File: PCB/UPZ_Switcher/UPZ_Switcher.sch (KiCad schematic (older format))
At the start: 0 parts

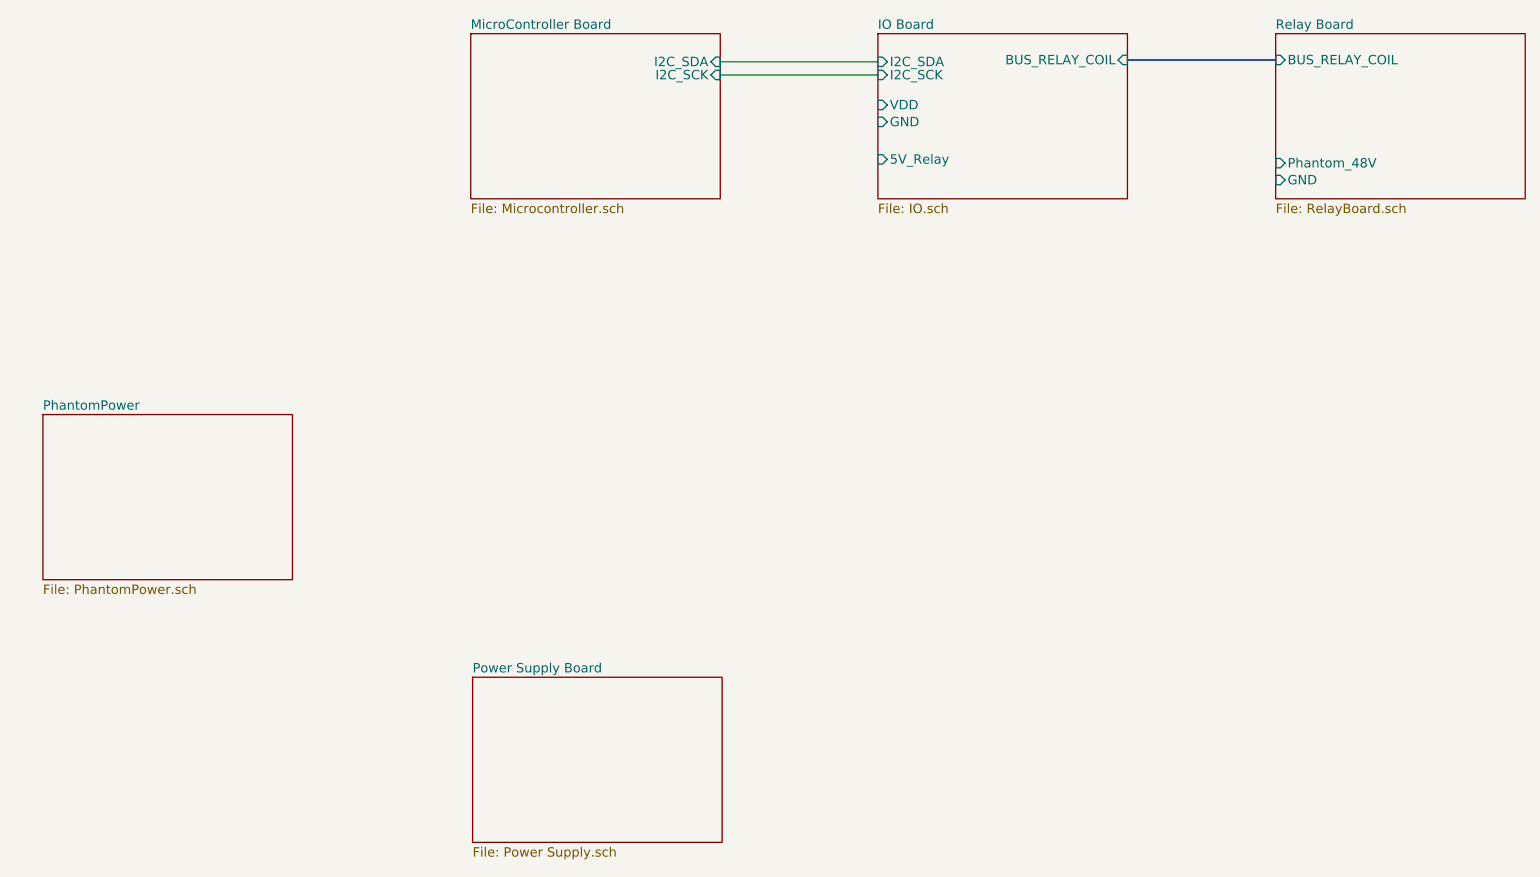
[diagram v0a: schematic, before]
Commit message: Updated schematic, PSU added + draft program
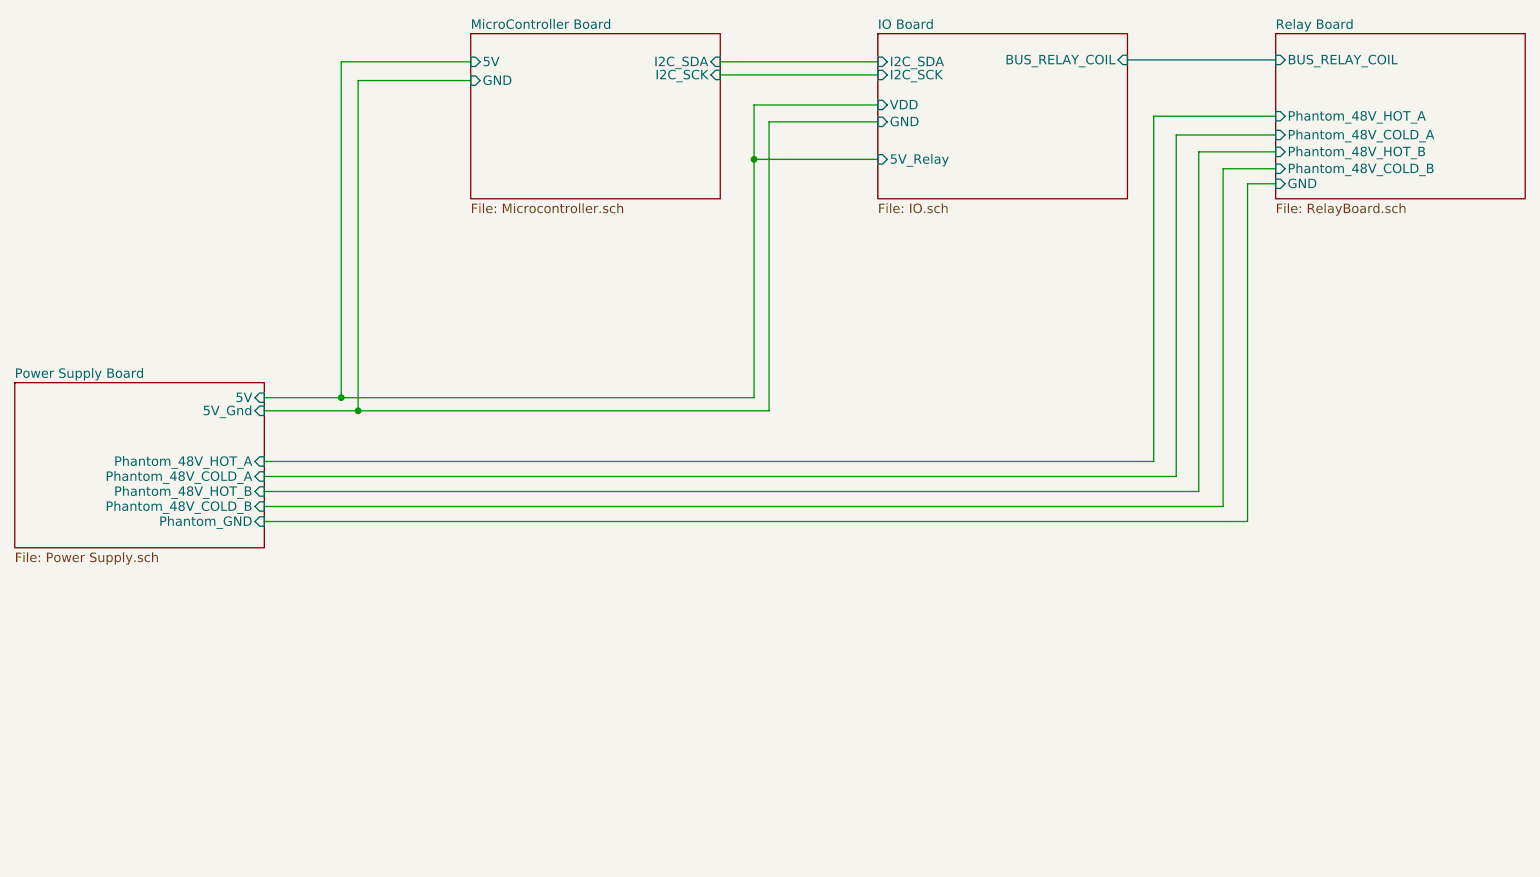
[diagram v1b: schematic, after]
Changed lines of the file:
@@
 $Descr A4 11693 8268
 encoding utf-8
-Sheet 1 6
+Sheet 1 5
 Title ""
 Date ""
@@
 F2 "I2C_SCK" I R 5270 1730 50
 F3 "I2C_SDA" I R 5270 1660 50
+F4 "5V" I L 3940 1660 50
+F5 "GND" I L 3940 1760 50
 $EndSheet
 $Sheet
-S 3950 4940 1330 880
+S 1510 3370 1330 880
 U 62E5E929
 F0 "Power Supply Board" 50
 F1 "Power Supply.sch" 50
+F2 "Phantom_48V_COLD_A" I R 2840 3870 50
+F3 "Phantom_48V_HOT_A" I R 2840 3790 50
+F4 "Phantom_48V_COLD_B" I R 2840 4030 50
+F5 "Phantom_48V_HOT_B" I R 2840 3950 50
+F6 "5V" I R 2840 3450 50
+F7 "Phantom_GND" I R 2840 4110 50
+F8 "5V_Gnd" I R 2840 3520 50
 $EndSheet
 $Sheet
@@
 F0 "Relay Board" 50
 F1 "RelayBoard.sch" 50
-F2 "Phantom_48V" I L 8230 2200 50
-F3 "BUS_RELAY_COIL" I L 8230 1650 50
-F4 "GND" I L 8230 2290 50
-$EndSheet
-$Sheet
-S 1660 3540 1330 880
-U 62E8A761
-F0 "PhantomPower" 50
-F1 "PhantomPower.sch" 50
+F2 "BUS_RELAY_COIL" I L 8230 1650 50
+F3 "GND" I L 8230 2310 50
+F4 "Phantom_48V_HOT_A" I L 8230 1950 50
+F5 "Phantom_48V_COLD_A" I L 8230 2050 50
+F6 "Phantom_48V_HOT_B" I L 8230 2140 50
+F7 "Phantom_48V_COLD_B" I L 8230 2230 50
 $EndSheet
 Wire Bus Line
@@
 Wire Wire Line
 	5270 1730 6110 1730
+Wire Wire Line
+	2840 3790 7580 3790
+Wire Wire Line
+	7580 3790 7580 1950
+Wire Wire Line
+	7580 1950 8230 1950
+Wire Wire Line
+	8230 2050 7700 2050
+Wire Wire Line
+	7700 2050 7700 3870
+Wire Wire Line
+	7700 3870 2840 3870
+Wire Wire Line
+	2840 3950 7820 3950
+Wire Wire Line
+	7820 3950 7820 2140
+Wire Wire Line
+	7820 2140 8230 2140
+Wire Wire Line
+	2840 4030 7950 4030
+Wire Wire Line
+	7950 4030 7950 2230
+Wire Wire Line
+	7950 2230 8230 2230
+Wire Wire Line
+	8230 2310 8080 2310
+Wire Wire Line
+	8080 2310 8080 4110
+Wire Wire Line
+	8080 4110 2840 4110
+Wire Wire Line
+	2840 3450 3250 3450
+Wire Wire Line
+	3250 3450 3250 1660
+Wire Wire Line
+	3250 1660 3940 1660
+Wire Wire Line
+	2840 3520 3340 3520
+Wire Wire Line
+	3340 3520 3340 1760
+Wire Wire Line
+	3340 1760 3940 1760
+Wire Wire Line
+	6110 1890 5450 1890
+Wire Wire Line
+	5450 1890 5450 2180
+Wire Wire Line
+	5450 3450 3250 3450
+Connection ~ 3250 3450
+Wire Wire Line
+	6110 1980 5530 1980
+Wire Wire Line
+	5530 1980 5530 3520
+Wire Wire Line
+	5530 3520 3340 3520
+Connection ~ 3340 3520
+Wire Wire Line
+	6110 2180 5450 2180
+Connection ~ 5450 2180
+Wire Wire Line
+	5450 2180 5450 3450
 $EndSCHEMATC

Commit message: Started PCB design
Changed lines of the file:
@@
 $Descr A4 11693 8268
 encoding utf-8
-Sheet 1 5
+Sheet 1 6
 Title ""
 Date ""
@@
 Comment4 ""
 $EndDescr
-$Sheet
-S 6110 1510 1330 880
-U 62DF27C2
-F0 "IO Board" 50
-F1 "IO.sch" 50
-F2 "BUS_RELAY_COIL" I R 7440 1650 50
-F3 "5V_Relay" I L 6110 2180 50
-F4 "I2C_SDA" I L 6110 1660 50
-F5 "I2C_SCK" I L 6110 1730 50
-F6 "VDD" I L 6110 1890 50
-F7 "GND" I L 6110 1980 50
-$EndSheet
 $Sheet
 S 3940 1510 1330 880
@@
 F8 "5V_Gnd" I R 2840 3520 50
 $EndSheet
-$Sheet
-S 8230 1510 1330 880
-U 62E5E978
-F0 "Relay Board" 50
-F1 "RelayBoard.sch" 50
-F2 "BUS_RELAY_COIL" I L 8230 1650 50
-F3 "GND" I L 8230 2310 50
-F4 "Phantom_48V_HOT_A" I L 8230 1950 50
-F5 "Phantom_48V_COLD_A" I L 8230 2050 50
-F6 "Phantom_48V_HOT_B" I L 8230 2140 50
-F7 "Phantom_48V_COLD_B" I L 8230 2230 50
-$EndSheet
-Wire Bus Line
-	7440 1650 8230 1650
 Wire Wire Line
-	5270 1660 6110 1660
+	2840 3790 5600 3790
 Wire Wire Line
-	5270 1730 6110 1730
+	2840 3950 5760 3950
 Wire Wire Line
-	2840 3790 7580 3790
-Wire Wire Line
-	7580 3790 7580 1950
-Wire Wire Line
-	7580 1950 8230 1950
-Wire Wire Line
-	8230 2050 7700 2050
-Wire Wire Line
-	7700 2050 7700 3870
-Wire Wire Line
-	7700 3870 2840 3870
-Wire Wire Line
-	2840 3950 7820 3950
-Wire Wire Line
-	7820 3950 7820 2140
-Wire Wire Line
-	7820 2140 8230 2140
-Wire Wire Line
-	2840 4030 7950 4030
-Wire Wire Line
-	7950 4030 7950 2230
-Wire Wire Line
-	7950 2230 8230 2230
-Wire Wire Line
-	8230 2310 8080 2310
-Wire Wire Line
-	8080 2310 8080 4110
-Wire Wire Line
-	8080 4110 2840 4110
+	2840 4030 5840 4030
 Wire Wire Line
 	2840 3450 3250 3450
@@
 	3340 1760 3940 1760
 Wire Wire Line
-	6110 1890 5450 1890
-Wire Wire Line
-	5450 1890 5450 2180
-Wire Wire Line
-	5450 3450 3250 3450
+	5440 3450 3250 3450
 Connection ~ 3250 3450
 Wire Wire Line
-	6110 1980 5530 1980
+	5520 3520 3340 3520
+Connection ~ 3340 3520
+$Sheet
+S 6110 2730 1330 880
+U 604B7458
+F0 "Main Relay Board" 50
+F1 "Main_Relay_Board.sch" 50
+F2 "Phantom_48V_HOT_A" I L 6110 3230 50
+F3 "Phantom_48V_COLD_A" I L 6110 3310 50
+F4 "Phantom_48V_HOT_B" I L 6110 3390 50
+F5 "Phantom_48V_COLD_B" I L 6110 3470 50
+F6 "Phantom_GND" I L 6110 3550 50
+F7 "I2C_SDA" I L 6110 2820 50
+F8 "I2C_SCK" I L 6110 2900 50
+F9 "VDD" I L 6110 2990 50
+F10 "GND" I L 6110 3070 50
+F11 "5V_Relay" I L 6110 3150 50
+$EndSheet
 Wire Wire Line
-	5530 1980 5530 3520
+	6110 3150 5440 3150
 Wire Wire Line
-	5530 3520 3340 3520
-Connection ~ 3340 3520
+	6110 3070 5520 3070
 Wire Wire Line
-	6110 2180 5450 2180
-Connection ~ 5450 2180
+	5520 3070 5520 3520
 Wire Wire Line
-	5450 2180 5450 3450
+	6110 3230 5600 3230
+Wire Wire Line
+	5600 3230 5600 3790
+Wire Wire Line
+	6110 3310 5680 3310
+Wire Wire Line
+	5680 3310 5680 3870
+Wire Wire Line
+	5680 3870 2840 3870
+Wire Wire Line
+	6110 3390 5760 3390
+Wire Wire Line
+	5760 3390 5760 3950
+Wire Wire Line
+	6110 3470 5840 3470
+Wire Wire Line
+	5840 3470 5840 4030
+Wire Wire Line
+	6110 3550 5920 3550
+Wire Wire Line
+	5920 3550 5920 4110
+Wire Wire Line
+	5920 4110 2840 4110
+Wire Wire Line
+	6110 2990 5440 2990
+Wire Wire Line
+	5440 2990 5440 3150
+Connection ~ 5440 3150
+Wire Wire Line
+	5440 3150 5440 3450
+Wire Wire Line
+	5270 1660 5760 1660
+Wire Wire Line
+	5760 1660 5760 2820
+Wire Wire Line
+	5760 2820 6110 2820
+Wire Wire Line
+	5270 1730 5700 1730
+Wire Wire Line
+	5700 1730 5700 2900
+Wire Wire Line
+	5700 2900 6110 2900
 $EndSCHEMATC

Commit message: Relay Board finished
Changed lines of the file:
@@
 F9 "VDD" I L 6110 2990 50
 F10 "GND" I L 6110 3070 50
-F11 "5V_Relay" I L 6110 3150 50
 $EndSheet
-Wire Wire Line
-	6110 3150 5440 3150
 Wire Wire Line
 	6110 3070 5520 3070
@@
 	6110 2990 5440 2990
 Wire Wire Line
-	5440 2990 5440 3150
-Connection ~ 5440 3150
-Wire Wire Line
-	5440 3150 5440 3450
-Wire Wire Line
 	5270 1660 5760 1660
 Wire Wire Line
@@
 Wire Wire Line
 	5700 2900 6110 2900
+Wire Wire Line
+	5440 2990 5440 3450
 $EndSCHEMATC
